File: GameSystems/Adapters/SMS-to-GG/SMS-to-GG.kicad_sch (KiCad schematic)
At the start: 2 parts, among them J1 Master System Fingers, J2 Game Gear Slot

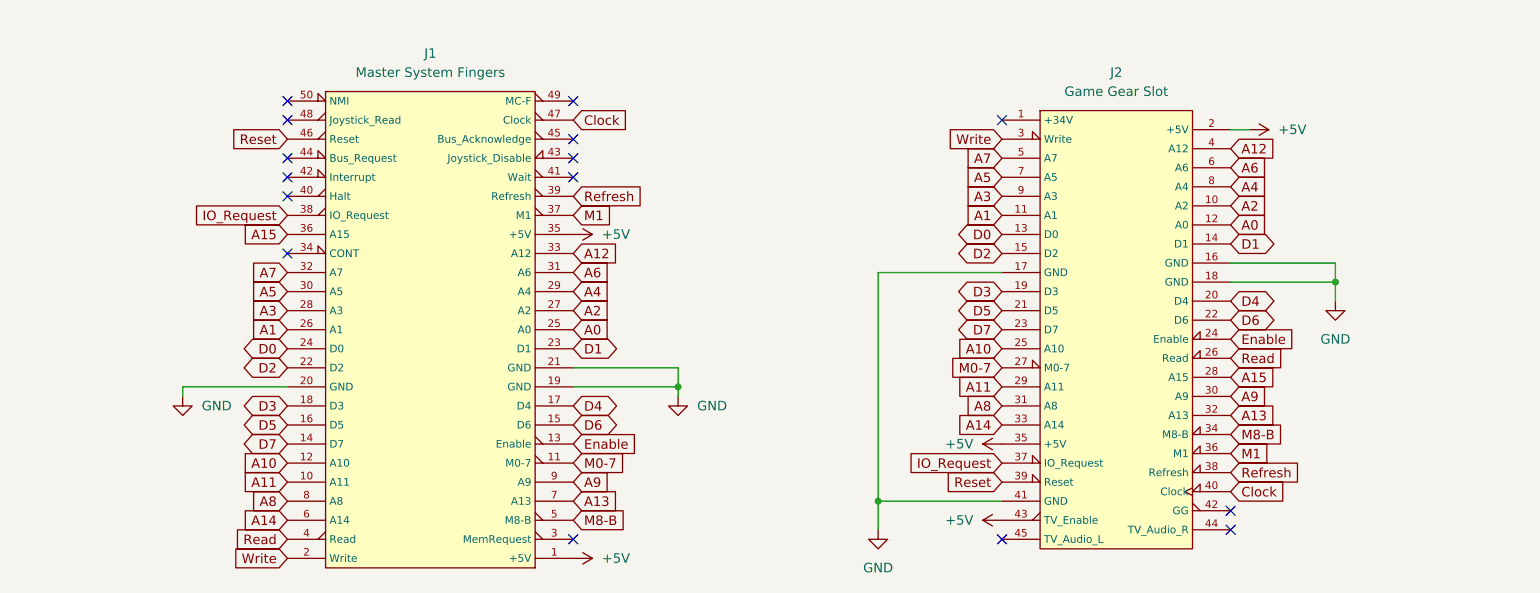
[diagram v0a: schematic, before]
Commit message: SMS-to-GG revisions + more
* Updated the SMS-to-GG adapter from Rev 2 to Rev 4.
  * Rev 3 (not in repository):
    * Moved GG slot footprint up to allow room for the RetroSix GG slot connector PCB.
    * Added RetroSix GG slot FPC header directly to PCB.
  * Rev 4:
    * Fixed silkscreen disclaimers to refer to SEGA (Japan).
    * Moved JLCPCB "Specify Location" text to under the FPC header.
    * Made some general cosmetic improvements.
    * Updated project files to Latest KiCad version.
* Reorganized the libraries a little.
* Added 2-hole version of the Game Gear slot.
* Updated `.gitignore` for new KiCad version and some plugins.
* Updated the disclaimers in the `README.md` files.
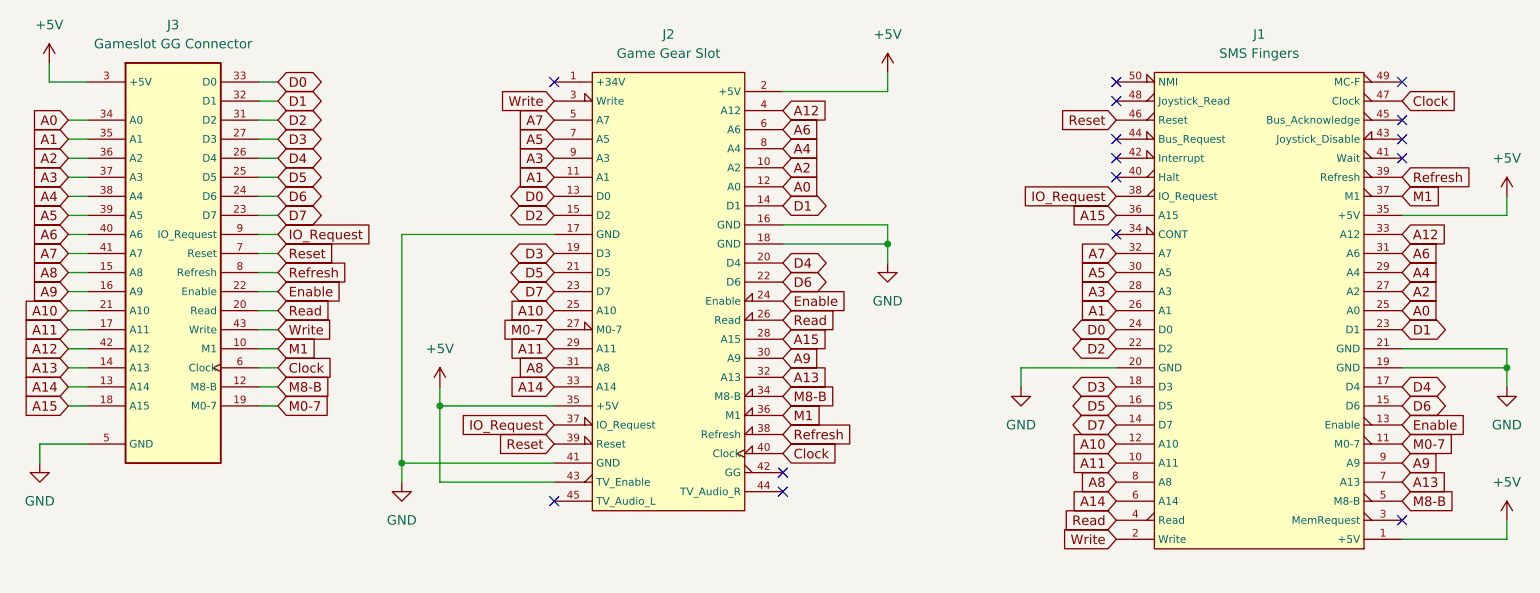
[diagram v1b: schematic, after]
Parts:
- added J3: Gameslot GG Connector, !MiscFootprints:FPC Connector - 45-pin - Multiple, symbol !SGSymbols:SG_GG_CARTRIDGE_SLOT_R6
- J1: value Master System Fingers -> SMS Fingers; Copyright ©2022 StarshadeRETRO -> ©2022-2024 StarshadeRETRO; Disclaimer SEGA and Master System are registered trademarks of SEGA GA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 -> SEGA is a registered trademark of SEGA CORPORATION (Japan).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
- J2: footprint !SGFootprints:SG_GG_CARTRIDGE_SLOT -> !SGFootprints:SG_GG_CARTRIDGE_SLOT_2H; Copyright ©2022 StarshadeRETRO -> ©2022-2024 StarshadeRETRO; Disclaimer SEGA and Game Gear are registered trademarks of SEGA GAMES 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 -> SEGA and Game Gear are registered trademarks of SEGA CORPOR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; now left out of the parts list
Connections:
- net +5V: now also J3.11 (+5V), J3.3 (+5V), J3.44 (+5V)
- net A0: now also J3.34 (A0)
- net A1: now also J3.35 (A1)
- net A10: now also J3.21 (A10)
- net A11: now also J3.17 (A11)
- net A12: now also J3.42 (A12)
- net A13: now also J3.14 (A13)
- net A14: now also J3.13 (A14)
- net A15: now also J3.18 (A15)
- net A2: now also J3.36 (A2)
- net A3: now also J3.37 (A3)
- net A4: now also J3.38 (A4)
- net A5: now also J3.39 (A5)
- net A6: now also J3.40 (A6)
- net A7: now also J3.41 (A7)
- net A8: now also J3.15 (A8)
- net A9: now also J3.16 (A9)
- net Clock: now also J3.6 (Clock)
- net D0: now also J3.33 (D0)
- net D1: now also J3.32 (D1)
- net D2: now also J3.31 (D2)
- net D3: now also J3.27 (D3)
- net D4: now also J3.26 (D4)
- net D5: now also J3.25 (D5)
- net D6: now also J3.24 (D6)
- net D7: now also J3.23 (D7)
- net Enable: now also J3.22 (Enable)
- net GND: now also J3.28 (GND), J3.29 (GND), J3.30 (GND), J3.5 (GND), J3.S1 (SHIELD), J3.S2 (SHIELD)
- net IO_Request: now also J3.9 (IO_Request)
- net M0-7: now also J3.19 (M0-7)
- net M1: now also J3.10 (M1)
- net M8-B: now also J3.12 (M8-B)
- net Read: now also J3.20 (Read)
- net Refresh: now also J3.8 (Refresh)
- net Reset: now also J3.7 (Reset)
- net Write: now also J3.43 (Write)
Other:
- company: ©2022 StarshadeRETRO; License: BSD-3-Clause -> ©2022-2024 StarshadeRETRO; License: BSD-3-Clause
- title: Sega Master System to Game Gear Adapter -> SEGA Master System to Game Gear Adapter
- moved on the sheet: J1, J2
